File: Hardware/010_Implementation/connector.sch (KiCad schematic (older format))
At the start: 9 parts, among them J2 Conn_01x09_Female, K1 G5V-2-DC5, K2 G5V-2-DC5, Q1 BC817

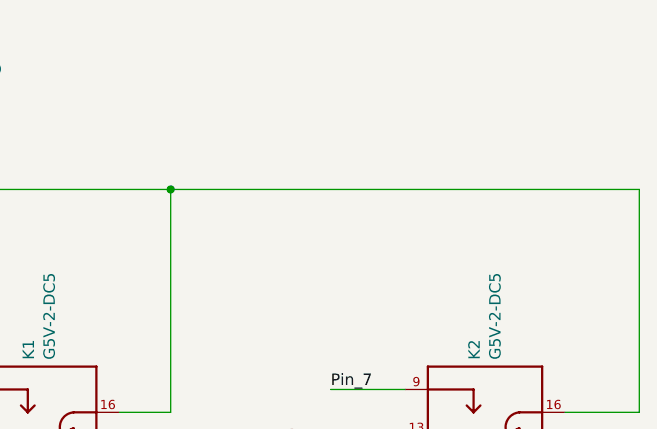
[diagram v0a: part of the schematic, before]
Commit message: Added Missing 5V marker
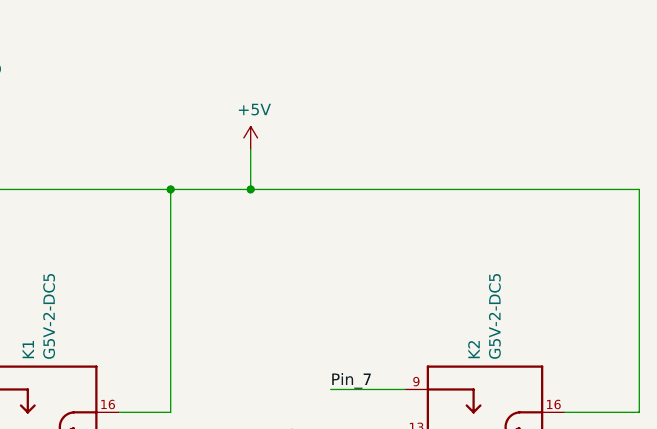
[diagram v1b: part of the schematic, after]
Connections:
- net +5V: now reaches D8.1 (K), K1.16, K2.16
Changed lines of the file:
@@
 	6450 4250 5650 4250
 Wire Wire Line
-	7900 1500 9950 1500
+	7900 1500 8250 1500
 Connection ~ 7900 1500
 Wire Wire Line
@@
 	1    0    0    -1
 $EndComp
+$Comp
+L power:+5V #PWR?
+U 1 1 5FA1A73B
+P 8250 1325
+F 0 "#PWR?" H 8250 1175 50  0001 C CNN
+F 1 "+5V" H 8265 1498 50  0000 C CNN
+F 2 "" H 8250 1325 50  0001 C CNN
+F 3 "" H 8250 1325 50  0001 C CNN
+	1    8250 1325
+	1    0    0    -1
+$EndComp
+Wire Wire Line
+	8250 1500 8250 1325
+Connection ~ 8250 1500
+Wire Wire Line
+	8250 1500 9950 1500
 $EndSCHEMATC

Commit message: Board version 4
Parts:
- renumbered D7 to D6, D8 to D7, J2 to J3, R13 to R16, R14 to R17, R15 to R18
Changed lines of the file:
@@
 Comment4 ""
 $EndDescr
-$Comp
-L Connector:Conn_01x09_Female J?
-U 1 1 5FA5ACF8
-P 1075 3775
-AR Path="/5F562A6B/5FA5ACF8" Ref="J?"  Part="1"
-AR Path="/5FA55ABF/5FA5ACF8" Ref="J2"  Part="1"
-F 0 "J2" H 967 3150 50  0000 C CNN
-F 1 "Conn_01x09_Female" H 967 3241 50  0000 C CNN
-F 2 "Connector_Dsub:DSUB-9_Female_Horizontal_P2.77x2.84mm_EdgePinOffset4.94mm_Housed_MountingHolesOffset7.48mm" H 1075 3775 50  0001 C CNN
-F 3 "~" H 1075 3775 50  0001 C CNN
-	1    1075 3775
-	-1   0    0    1
-$EndComp
 Text Label 1725 2650 3    50   ~ 0
 OBD_VDD
-NoConn ~ 1275 3475
-NoConn ~ 1275 3675
-NoConn ~ 1275 3875
-NoConn ~ 1275 4175
 Text HLabel 1725 1350 1    50   Output ~ 0
 OBD_VDD
@@
 $EndComp
 $Comp
-L Diode:1N4148 D8
+L Diode:1N4148 D7
 U 1 1 5FB2B4A7
 P 5650 2775
-F 0 "D8" V 5604 2855 50  0000 L CNN
+F 0 "D7" V 5604 2855 50  0000 L CNN
 F 1 "1N4148" V 5695 2855 50  0000 L CNN
 F 2 "Diode_THT:D_DO-35_SOD27_P7.62mm_Horizontal" H 5650 2600 50  0001 C CNN
@@
 	7450 4450 7450 4850
 $Comp
-L power:GND #PWR020
+L power:GND #PWR023
 U 1 1 5FB36BEA
 P 7450 4850
-F 0 "#PWR020" H 7450 4600 50  0001 C CNN
+F 0 "#PWR023" H 7450 4600 50  0001 C CNN
 F 1 "GND" H 7455 4677 50  0000 C CNN
 F 2 "" H 7450 4850 50  0001 C CNN
@@
 $EndComp
 $Comp
-L Device:R R15
+L Device:R R18
 U 1 1 5FB372EA
 P 6950 4600
-F 0 "R15" H 7020 4646 50  0000 L CNN
+F 0 "R18" H 7020 4646 50  0000 L CNN
 F 1 "150" H 7020 4555 50  0000 L CNN
 F 2 "Resistor_SMD:R_0805_2012Metric_Pad1.15x1.40mm_HandSolder" V 6880 4600 50  0001 C CNN
@@
 $EndComp
 $Comp
-L Device:R R14
+L Device:R R17
 U 1 1 5FB379FD
 P 6600 4250
-F 0 "R14" V 6393 4250 50  0000 C CNN
+F 0 "R17" V 6393 4250 50  0000 C CNN
 F 1 "430" V 6484 4250 50  0000 C CNN
 F 2 "Resistor_SMD:R_0805_2012Metric_Pad1.15x1.40mm_HandSolder" V 6530 4250 50  0001 C CNN
@@
 	6950 4250 7150 4250
 $Comp
-L power:GND #PWR019
+L power:GND #PWR022
 U 1 1 5FB38603
 P 6950 4850
-F 0 "#PWR019" H 6950 4600 50  0001 C CNN
+F 0 "#PWR022" H 6950 4600 50  0001 C CNN
 F 1 "GND" H 6955 4677 50  0000 C CNN
 F 2 "" H 6950 4850 50  0001 C CNN
@@
 	2675 4425 2675 750
 $Comp
-L power:GND #PWR018
+L power:GND #PWR021
 U 1 1 5FB4D7F5
 P 6475 3125
-F 0 "#PWR018" H 6475 2875 50  0001 C CNN
+F 0 "#PWR021" H 6475 2875 50  0001 C CNN
 F 1 "GND" H 6480 2952 50  0000 C CNN
 F 2 "" H 6475 3125 50  0001 C CNN
@@
 P 4050 5675
 AR Path="/5F52F099/5FB5FD23" Ref="D?"  Part="1"
-AR Path="/5FA55ABF/5FB5FD23" Ref="D7"  Part="1"
-F 0 "D7" V 4089 5557 50  0000 R CNN
+AR Path="/5FA55ABF/5FB5FD23" Ref="D6"  Part="1"
+F 0 "D6" V 4089 5557 50  0000 R CNN
 F 1 "RED" V 3998 5557 50  0000 R CNN
 F 2 "LED_THT:LED_D3.0mm" H 4050 5675 50  0001 C CNN
@@
 P 4050 6150
 AR Path="/5F52F099/5FB5FD29" Ref="R?"  Part="1"
-AR Path="/5FA55ABF/5FB5FD29" Ref="R13"  Part="1"
-F 0 "R13" H 4120 6196 50  0000 L CNN
+AR Path="/5FA55ABF/5FB5FD29" Ref="R16"  Part="1"
+F 0 "R16" H 4120 6196 50  0000 L CNN
 F 1 "500" H 4120 6105 50  0000 L CNN
 F 2 "Resistor_SMD:R_0805_2012Metric_Pad1.15x1.40mm_HandSolder" V 3980 6150 50  0001 C CNN
@@
 	4050 6300 4050 6875
 $Comp
-L power:+3.3V #PWR017
+L power:+3.3V #PWR020
 U 1 1 5FB62F1D
 P 4050 5200
-F 0 "#PWR017" H 4050 5050 50  0001 C CNN
+F 0 "#PWR020" H 4050 5050 50  0001 C CNN
 F 1 "+3.3V" H 4065 5373 50  0000 C CNN
 F 2 "" H 4050 5200 50  0001 C CNN
@@
 $EndComp
 $Comp
-L power:+5V #PWR023
+L power:+5V #PWR024
 U 1 1 5FA1A73B
 P 8250 1325
-F 0 "#PWR023" H 8250 1175 50  0001 C CNN
+F 0 "#PWR024" H 8250 1175 50  0001 C CNN
 F 1 "+5V" H 8265 1498 50  0000 C CNN
 F 2 "" H 8250 1325 50  0001 C CNN
@@
 Wire Wire Line
 	8250 1500 9950 1500
+NoConn ~ 1275 4175
+NoConn ~ 1275 3875
+NoConn ~ 1275 3475
+NoConn ~ 1275 3675
+$Comp
+L Connector:Conn_01x09_Female J?
+U 1 1 5FA5ACF8
+P 1075 3775
+AR Path="/5F562A6B/5FA5ACF8" Ref="J?"  Part="1"
+AR Path="/5FA55ABF/5FA5ACF8" Ref="J3"  Part="1"
+F 0 "J3" H 967 3150 50  0000 C CNN
+F 1 "Conn_01x09_Female" H 967 3241 50  0000 C CNN
+F 2 "Connector_Dsub:DSUB-9_Female_Horizontal_P2.77x2.84mm_EdgePinOffset4.94mm_Housed_MountingHolesOffset7.48mm" H 1075 3775 50  0001 C CNN
+F 3 "~" H 1075 3775 50  0001 C CNN
+	1    1075 3775
+	-1   0    0    1
+$EndComp
 $EndSCHEMATC

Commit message: Board Version 4.2
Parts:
- added C11: 100n, symbol Device:C
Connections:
- net +5V: now also C11.1
- net GND: now also C11.2
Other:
- note added: "ON when CAN is Active\nOFF when OBD ist Active"
- note added: "~OBD~/CAN"
- moved on the sheet: D7, K1, K2, Q1, R17, R18

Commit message: Board Version 5
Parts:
- C11: footprint (none) -> Capacitor_SMD:C_0603_1608Metric_Pad1.08x0.95mm_HandSolder
- D6: Vorhanden (none) -> Yes
- J3: value Conn_01x09_Female -> DSUB9; Vorhanden (none) -> Yes
- K1, K2: Field4 Omron Electronics -> (none)
- R16, R17, R18: footprint Resistor_SMD:R_0805_2012Metric_Pad1.15x1.40mm_HandSolder -> Resistor_SMD:R_0603_1608Metric_Pad0.98x0.95mm_HandSolder
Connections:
- net OBD-CAN_Switch renamed ~OBD~\CAN
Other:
- note removed: "~OBD~/CAN"
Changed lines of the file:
@@
 	725  4425 2675 4425
 Text HLabel 6695 4515 0    50   Input ~ 0
-OBD-CAN_Switch
+~OBD~\CAN
 $Comp
 L Board:G5V-2-DC5 K2
@@
 F 2 "Board:RELAY_G5V-2-DC5" H 9730 2620 50  0001 L BNN
 F 3 "Relay; E-Mech; Low Signal; DPDT; Cur-Rtg 0.5/2AAC/ADC; Ctrl-V 5DC; Vol-Rtg 125/30AC/DC" H 9730 2620 50  0001 L BNN
-F 4 "Omron Electronics" H 9730 2620 50  0001 L BNN "Field4"
+F 4 "" H 9730 2620 50  0001 L BNN "Field4"
 F 5 "QFN-68 Omron" H 9730 2620 50  0001 L BNN "Field5"
 F 6 "Unavailable" H 9730 2620 50  0001 L BNN "Field6"
@@
 F 0 "R18" H 8065 4911 50  0000 L CNN
 F 1 "150" H 8065 4820 50  0000 L CNN
-F 2 "Resistor_SMD:R_0805_2012Metric_Pad1.15x1.40mm_HandSolder" V 7925 4865 50  0001 C CNN
+F 2 "Resistor_SMD:R_0603_1608Metric_Pad0.98x0.95mm_HandSolder" V 7925 4865 50  0001 C CNN
 F 3 "~" H 7995 4865 50  0001 C CNN
 	1    7995 4865
@@
 F 0 "R17" V 7438 4515 50  0000 C CNN
 F 1 "430" V 7529 4515 50  0000 C CNN
-F 2 "Resistor_SMD:R_0805_2012Metric_Pad1.15x1.40mm_HandSolder" V 7575 4515 50  0001 C CNN
+F 2 "Resistor_SMD:R_0603_1608Metric_Pad0.98x0.95mm_HandSolder" V 7575 4515 50  0001 C CNN
 F 3 "~" H 7645 4515 50  0001 C CNN
 	1    7645 4515
@@
 F 2 "LED_THT:LED_D3.0mm" H 4050 5675 50  0001 C CNN
 F 3 "~" H 4050 5675 50  0001 C CNN
+F 4 "Yes" H 4050 5675 50  0001 C CNN "Vorhanden"
 	1    4050 5675
 	0    -1   -1   0
@@
 F 0 "R16" H 4120 6196 50  0000 L CNN
 F 1 "500" H 4120 6105 50  0000 L CNN
-F 2 "Resistor_SMD:R_0805_2012Metric_Pad1.15x1.40mm_HandSolder" V 3980 6150 50  0001 C CNN
+F 2 "Resistor_SMD:R_0603_1608Metric_Pad0.98x0.95mm_HandSolder" V 3980 6150 50  0001 C CNN
 F 3 "~" H 4050 6150 50  0001 C CNN
 	1    4050 6150
@@
 AR Path="/5FA55ABF/5FA5ACF8" Ref="J3"  Part="1"
 F 0 "J3" H 967 3150 50  0000 C CNN
-F 1 "Conn_01x09_Female" H 967 3241 50  0000 C CNN
+F 1 "DSUB9" H 967 3241 50  0000 C CNN
 F 2 "Connector_Dsub:DSUB-9_Female_Horizontal_P2.77x2.84mm_EdgePinOffset4.94mm_Housed_MountingHolesOffset7.48mm" H 1075 3775 50  0001 C CNN
 F 3 "~" H 1075 3775 50  0001 C CNN
+F 4 "Yes" H 1075 3775 50  0001 C CNN "Vorhanden"
 	1    1075 3775
 	-1   0    0    1
@@
 Text Notes 4360 5710 0    50   ~ 0
 ON when CAN is Active\nOFF when OBD ist Active
-Text Notes 6225 4410 0    50   ~ 0
-~OBD~/CAN
 $Comp
 L Device:C C11
@@
 F 0 "C11" H 8680 1701 50  0000 R CNN
 F 1 "100n" H 8680 1610 50  0000 R CNN
-F 2 "" H 8833 1505 50  0001 C CNN
+F 2 "Capacitor_SMD:C_0603_1608Metric_Pad1.08x0.95mm_HandSolder" H 8833 1505 50  0001 C CNN
 F 3 "~" H 8795 1655 50  0001 C CNN
 	1    8795 1655
@@
 F 2 "Board:RELAY_G5V-2-DC5" H 7745 2615 50  0001 L BNN
 F 3 "Relay; E-Mech; Low Signal; DPDT; Cur-Rtg 0.5/2AAC/ADC; Ctrl-V 5DC; Vol-Rtg 125/30AC/DC" H 7745 2615 50  0001 L BNN
-F 4 "Omron Electronics" H 7745 2615 50  0001 L BNN "Field4"
+F 4 "" H 7745 2615 50  0001 L BNN "Field4"
 F 5 "QFN-68 Omron" H 7745 2615 50  0001 L BNN "Field5"
 F 6 "Unavailable" H 7745 2615 50  0001 L BNN "Field6"

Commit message: Board Version 7
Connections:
- net BUS_H: now also K2.4; no longer K2.13
- net BUS_L: now also K2.13; no longer K2.4
- net Pin_2: now also K2.9; no longer K2.8
- net Pin_3: now also K2.6; no longer K2.11
- net Pin_5: now also K2.11; no longer K2.6
- net Pin_7: now also K2.8; no longer K2.9
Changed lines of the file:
@@
 Text Notes 1510 2935 2    50   ~ 0
 DSUB-9 Connector\n
+Text HLabel 10455 2820 2    50   BiDi ~ 0
+BUS_H
 Text HLabel 10455 2320 2    50   BiDi ~ 0
-BUS_H
-Text HLabel 10455 2820 2    50   BiDi ~ 0
 BUS_L
 Wire Wire Line
@@
 Pin_2
 Wire Wire Line
-	10130 2320 10455 2320
+	10130 2820 10455 2820
 Wire Wire Line
-	10130 2120 10455 2120
-Text Label 10455 2120 2    50   ~ 0
+	10130 2620 10455 2620
+Text Label 10455 2620 2    50   ~ 0
 Pin_7
 Wire Wire Line
-	10130 2520 10455 2520
-Text Label 10455 2520 2    50   ~ 0
+	10130 3020 10455 3020
+Text Label 10455 3020 2    50   ~ 0
 Pin_3
 Wire Wire Line
-	10130 2820 10455 2820
+	10130 2320 10455 2320
 Wire Notes Line
 	2675 4425 2675 750
@@
 $EndComp
 Wire Wire Line
-	10130 2620 10455 2620
+	10130 2120 10455 2120
 Wire Wire Line
-	10130 3020 10455 3020
-Text Label 10455 2620 2    50   ~ 0
+	10130 2520 10455 2520
+Text Label 10455 2120 2    50   ~ 0
 Pin_2
-Text Label 10455 3020 2    50   ~ 0
+Text Label 10455 2520 2    50   ~ 0
 Pin_5
 Text Notes 5975 1175 0    50   ~ 0

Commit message: Moved Pi-Filter to the top section. Added alignment marks on the back layer.
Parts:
- J3: footprint Connector_Dsub:DSUB-9_Female_Horizontal_P2.77x2.84mm_EdgePinOffset4.94mm_Housed_MountingHolesOffset7.48mm -> Connector_Dsub:DSUB-9_Male_Horizontal_P2.77x2.84mm_EdgePinOffset4.94mm_Housed_MountingHolesOffset7.48mm
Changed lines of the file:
@@
 F 0 "J3" H 967 3150 50  0000 C CNN
 F 1 "DSUB9" H 967 3241 50  0000 C CNN
-F 2 "Connector_Dsub:DSUB-9_Female_Horizontal_P2.77x2.84mm_EdgePinOffset4.94mm_Housed_MountingHolesOffset7.48mm" H 1075 3775 50  0001 C CNN
+F 2 "Connector_Dsub:DSUB-9_Male_Horizontal_P2.77x2.84mm_EdgePinOffset4.94mm_Housed_MountingHolesOffset7.48mm" H 1075 3775 50  0001 C CNN
 F 3 "~" H 1075 3775 50  0001 C CNN
 F 4 "Yes" H 1075 3775 50  0001 C CNN "Vorhanden"

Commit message: Board version 8 with gerber files
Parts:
- added C18: 100n, Capacitor_SMD:C_0603_1608Metric_Pad1.08x0.95mm_HandSolder, symbol Device:C
- added D9: 1N4148, Diode_THT:D_DO-35_SOD27_P7.62mm_Horizontal, symbol Diode:1N4148
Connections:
- net +5V: now also C18.1, D9.1 (K)
- net GND: now also C18.2
- net at D7.2 (A), K1.1, K2.1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: now also D9.2 (A)
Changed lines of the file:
@@
 Wire Wire Line
 	8795 1505 8795 1470
-Wire Wire Line
-	8795 1470 8530 1470
 Connection ~ 8530 1470
 Wire Wire Line
@@
 	8725 2215 9105 2215
 Wire Wire Line
-	8045 2215 8530 2215
+	8045 2215 8298 2215
 Wire Wire Line
 	8530 1470 8530 2215
@@
 Wire Wire Line
 	8530 2215 8725 2215
+$Comp
+L Diode:1N4148 D9
+U 1 1 5FBF12D3
+P 8297 2773
+F 0 "D9" V 8251 2853 50  0000 L CNN
+F 1 "1N4148" V 8342 2853 50  0000 L CNN
+F 2 "Diode_THT:D_DO-35_SOD27_P7.62mm_Horizontal" H 8297 2598 50  0001 C CNN
+F 3 "https://assets.nexperia.com/documents/data-sheet/1N4148_1N4448.pdf" H 8297 2773 50  0001 C CNN
+	1    8297 2773
+	0    1    1    0
+$EndComp
+Wire Wire Line
+	8297 2623 8298 2623
+Wire Wire Line
+	8298 2623 8298 2215
+Connection ~ 8298 2215
+Wire Wire Line
+	8298 2215 8530 2215
+Wire Wire Line
+	8297 2923 8297 3015
+Wire Wire Line
+	8297 3015 8245 3015
+Connection ~ 8245 3015
+$Comp
+L Device:C C18
+U 1 1 5FBF7A1C
+P 9341 1653
+F 0 "C18" H 9226 1699 50  0000 R CNN
+F 1 "100n" H 9226 1608 50  0000 R CNN
+F 2 "Capacitor_SMD:C_0603_1608Metric_Pad1.08x0.95mm_HandSolder" H 9379 1503 50  0001 C CNN
+F 3 "~" H 9341 1653 50  0001 C CNN
+	1    9341 1653
+	-1   0    0    -1
+$EndComp
+$Comp
+L power:GND #PWR0105
+U 1 1 5FBF7A22
+P 9341 1878
+F 0 "#PWR0105" H 9341 1628 50  0001 C CNN
+F 1 "GND" H 9346 1705 50  0000 C CNN
+F 2 "" H 9341 1878 50  0001 C CNN
+F 3 "" H 9341 1878 50  0001 C CNN
+	1    9341 1878
+	1    0    0    -1
+$EndComp
+Wire Wire Line
+	9341 1803 9341 1878
+Wire Wire Line
+	9341 1503 9341 1470
+Wire Wire Line
+	8530 1470 8795 1470
+Connection ~ 8795 1470
+Wire Wire Line
+	8795 1470 9341 1470
 $EndSCHEMATC
